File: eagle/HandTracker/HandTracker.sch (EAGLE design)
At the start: 29 parts, among them IC1 FT232RL, J1 ZX62-AB-5PA(31), U1 LSM9DS1TR, U2 MAX11629EEE+21-0055_E16+5_MXM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

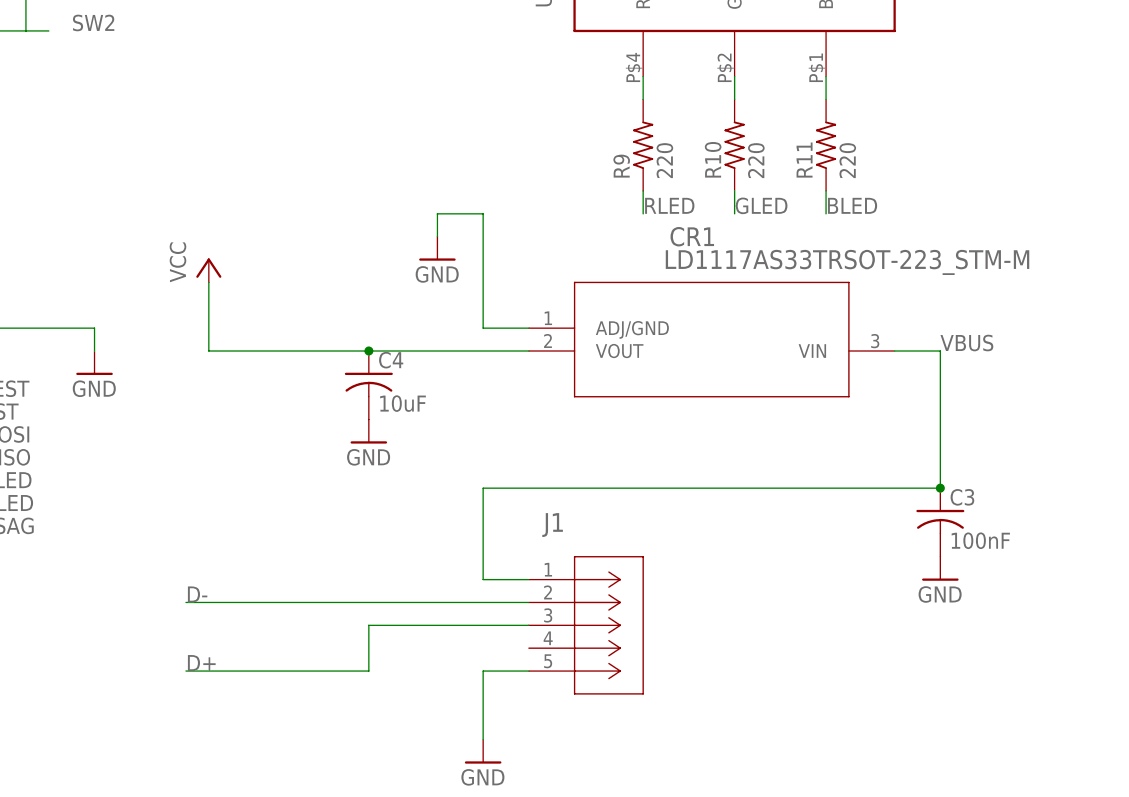
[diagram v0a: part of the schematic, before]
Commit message: Changed linear voltage regulator.
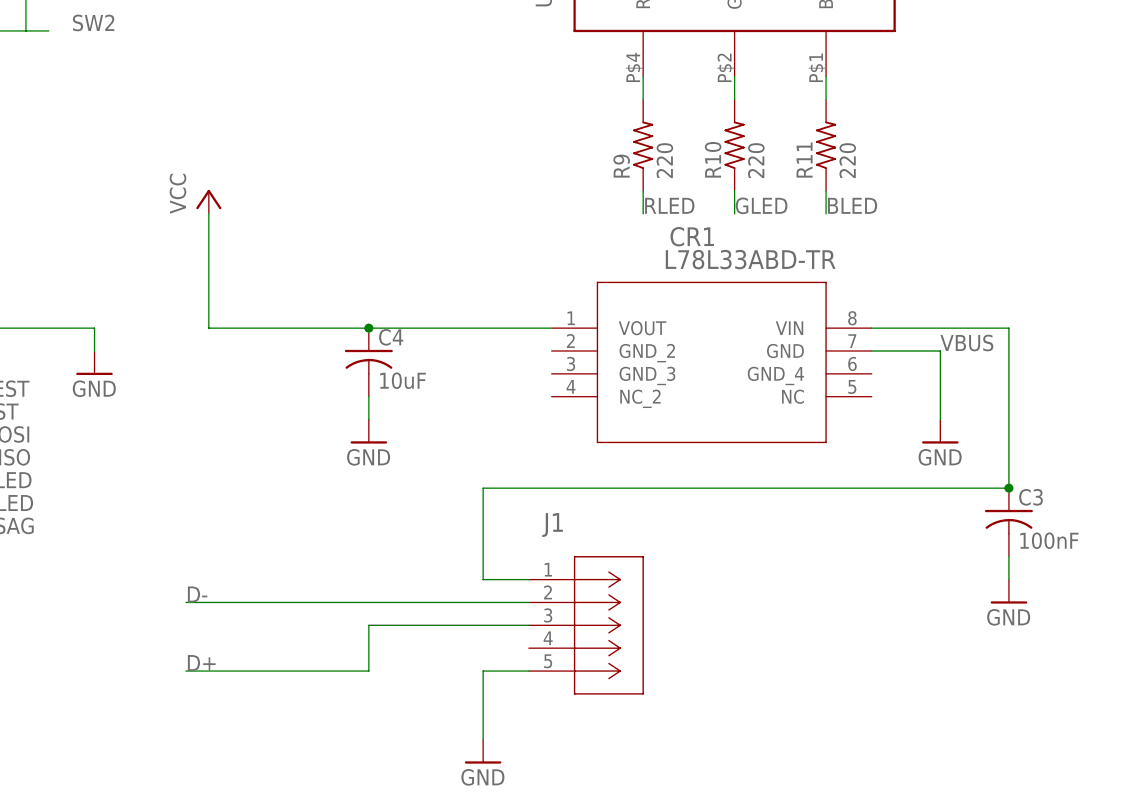
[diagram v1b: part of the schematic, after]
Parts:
- CR1: value LD1117AS33TRSOT-223_STM-M -> L78L33ABD-TR; device LD1117AS33TR:LD1117AS33TRSOT-223_STM-M -> Regulator:L78L33ABD-TR
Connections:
- net GND: now also CR1.GND; no longer CR1.ADJ/GND
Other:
- moved on the sheet: C3, C4
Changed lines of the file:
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@@
 <drawing>
 <settings>
-<setting alwaysvectorfont="no"/>
+<setting alwaysvectorfont="yes"/>
 <setting verticaltext="up"/>
 </settings>
@@
 <parts>
 <part name="U$1" library="ELEC327" deviceset="MSP430G2XX3" device="TSSOP"/>
-<part name="CR1" library="LD1117AS33TR" deviceset="LD1117AS33TR" device="SOT-223_STM-M"/>
 <part name="U1" library="LSM9DS1" deviceset="LSM9DS1TR" device=""/>
 <part name="U2" library="MAX11629EEE+" deviceset="MAX11629EEE+" device="21-0055_E16+5_MXM-M"/>
@@
 <part name="C9" library="rcl" library_urn="urn:adsk.eagle:library:334" deviceset="C-US" device="C1206" package3d_urn="urn:adsk.eagle:package:23618/2" value="10nF"/>
 <part name="GND15" library="supply1" library_urn="urn:adsk.eagle:library:371" deviceset="GND" device=""/>
+<part name="CR1" library="Regulator" deviceset="L78L33ABD-TR" device=""/>
 </parts>
 <sheets>
@@
 <attribute name="NAME" x="40.64" y="-33.02" size="1.778" layer="95"/>
 </instance>
-<instance part="CR1" gate="A" x="139.7" y="-10.16" smashed="yes">
-<attribute name="NAME" x="157.8356" y="-1.0414" size="2.0828" layer="95" ratio="6" rot="SR0"/>
-<attribute name="VALUE" x="157.2006" y="-3.5814" size="2.0828" layer="96" ratio="6" rot="SR0"/>
-</instance>
 <instance part="U1" gate="A" x="-66.04" y="-27.94" smashed="yes">
 <attribute name="NAME" x="-40.2844" y="-18.8214" size="2.0828" layer="95" ratio="6" rot="SR0"/>
@@
 <attribute name="VALUE" x="134.62" y="-60.96" size="1.778" layer="96"/>
 </instance>
-<instance part="GND2" gate="1" x="132.08" y="-2.54" smashed="yes">
-<attribute name="VALUE" x="129.54" y="-5.08" size="1.778" layer="96"/>
-</instance>
-<instance part="P+1" gate="VCC" x="106.68" y="-2.54" smashed="yes">
-<attribute name="VALUE" x="104.14" y="-5.08" size="1.778" layer="96" rot="R90"/>
+<instance part="GND2" gate="1" x="187.96" y="-22.86" smashed="yes">
+<attribute name="VALUE" x="185.42" y="-25.4" size="1.778" layer="96"/>
+</instance>
+<instance part="P+1" gate="VCC" x="106.68" y="5.08" smashed="yes">
+<attribute name="VALUE" x="104.14" y="2.54" size="1.778" layer="96" rot="R90"/>
 </instance>
 <instance part="P+2" gate="VCC" x="25.4" y="-5.08" smashed="yes">
@@
 <attribute name="VALUE" x="-5.08" y="17.78" size="1.778" layer="96"/>
 </instance>
-<instance part="C3" gate="G$1" x="187.96" y="-30.48" smashed="yes">
-<attribute name="NAME" x="188.976" y="-29.845" size="1.778" layer="95"/>
-<attribute name="VALUE" x="188.976" y="-34.671" size="1.778" layer="96"/>
-</instance>
-<instance part="GND9" gate="1" x="187.96" y="-38.1" smashed="yes">
-<attribute name="VALUE" x="185.42" y="-40.64" size="1.778" layer="96"/>
-</instance>
-<instance part="C4" gate="G$1" x="124.46" y="-15.24" smashed="yes">
-<attribute name="NAME" x="125.476" y="-14.605" size="1.778" layer="95"/>
-<attribute name="VALUE" x="125.476" y="-19.431" size="1.778" layer="96"/>
+<instance part="C3" gate="G$1" x="195.58" y="-30.48" smashed="yes">
+<attribute name="NAME" x="196.596" y="-29.845" size="1.778" layer="95"/>
+<attribute name="VALUE" x="196.596" y="-34.671" size="1.778" layer="96"/>
+</instance>
+<instance part="GND9" gate="1" x="195.58" y="-40.64" smashed="yes">
+<attribute name="VALUE" x="193.04" y="-43.18" size="1.778" layer="96"/>
+</instance>
+<instance part="C4" gate="G$1" x="124.46" y="-12.7" smashed="yes">
+<attribute name="NAME" x="125.476" y="-12.065" size="1.778" layer="95"/>
+<attribute name="VALUE" x="125.476" y="-16.891" size="1.778" layer="96"/>
 </instance>
 <instance part="GND10" gate="1" x="124.46" y="-22.86" smashed="yes">
@@
 <instance part="GND15" gate="1" x="10.16" y="-48.26" smashed="yes">
 <attribute name="VALUE" x="7.62" y="-50.8" size="1.778" layer="96"/>
+</instance>
+<instance part="CR1" gate="A" x="142.24" y="-10.16" smashed="yes">
+<attribute name="NAME" x="157.8356" y="-1.0414" size="2.0828" layer="95" ratio="6" rot="SR0"/>
+<attribute name="VALUE" x="157.2006" y="-3.5814" size="2.0828" layer="96" ratio="6" rot="SR0"/>
 </instance>
 </instances>
@@
 <nets>
 <net name="GND" class="0">
-<segment>
-<pinref part="CR1" gate="A" pin="ADJ/GND"/>
-<wire x1="142.24" y1="-10.16" x2="137.16" y2="-10.16" width="0.1524" layer="91"/>
-<wire x1="137.16" y1="-10.16" x2="137.16" y2="2.54" width="0.1524" layer="91"/>
-<wire x1="137.16" y1="2.54" x2="132.08" y2="2.54" width="0.1524" layer="91"/>
-<pinref part="GND2" gate="1" pin="GND"/>
-<wire x1="132.08" y1="2.54" x2="132.08" y2="0" width="0.1524" layer="91"/>
-</segment>
 <segment>
 <pinref part="J1" gate="A" pin="GND"/>
@@
 <pinref part="C3" gate="G$1" pin="2"/>
 <pinref part="GND9" gate="1" pin="GND"/>
+<wire x1="195.58" y1="-35.56" x2="195.58" y2="-38.1" width="0.1524" layer="91"/>
 </segment>
 <segment>
 <pinref part="C4" gate="G$1" pin="2"/>
 <pinref part="GND10" gate="1" pin="GND"/>
+<wire x1="124.46" y1="-17.78" x2="124.46" y2="-20.32" width="0.1524" layer="91"/>
 </segment>
 <segment>
@@
 <pinref part="GND15" gate="1" pin="GND"/>
 </segment>
+<segment>
+<pinref part="GND2" gate="1" pin="GND"/>
+<wire x1="187.96" y1="-20.32" x2="187.96" y2="-12.7" width="0.1524" layer="91"/>
+<pinref part="CR1" gate="A" pin="GND"/>
+<wire x1="187.96" y1="-12.7" x2="180.34" y2="-12.7" width="0.1524" layer="91"/>
+</segment>
 </net>
 <net name="VBUS" class="0">
@@
 <wire x1="142.24" y1="-38.1" x2="137.16" y2="-38.1" width="0.1524" layer="91"/>
 <wire x1="137.16" y1="-38.1" x2="137.16" y2="-27.94" width="0.1524" layer="91"/>
-<wire x1="137.16" y1="-27.94" x2="187.96" y2="-27.94" width="0.1524" layer="91"/>
+<wire x1="137.16" y1="-27.94" x2="195.58" y2="-27.94" width="0.1524" layer="91"/>
+<wire x1="195.58" y1="-27.94" x2="195.58" y2="-10.16" width="0.1524" layer="91"/>
+<wire x1="195.58" y1="-10.16" x2="180.34" y2="-10.16" width="0.1524" layer="91"/>
+<pinref part="C3" gate="G$1" pin="1"/>
+<junction x="195.58" y="-27.94"/>
+<label x="187.96" y="-12.7" size="1.778" layer="95"/>
 <pinref part="CR1" gate="A" pin="VIN"/>
-<wire x1="187.96" y1="-27.94" x2="187.96" y2="-12.7" width="0.1524" layer="91"/>
-<wire x1="187.96" y1="-12.7" x2="182.88" y2="-12.7" width="0.1524" layer="91"/>
-<pinref part="C3" gate="G$1" pin="1"/>
-<junction x="187.96" y="-27.94"/>
-<label x="187.96" y="-12.7" size="1.778" layer="95"/>
 </segment>
 <segment>
@@
 <segment>
 <pinref part="P+1" gate="VCC" pin="VCC"/>
-<wire x1="106.68" y1="-5.08" x2="106.68" y2="-12.7" width="0.1524" layer="91"/>
+<wire x1="106.68" y1="2.54" x2="106.68" y2="-10.16" width="0.1524" layer="91"/>
+<wire x1="106.68" y1="-10.16" x2="124.46" y2="-10.16" width="0.1524" layer="91"/>
+<pinref part="C4" gate="G$1" pin="1"/>
+<wire x1="124.46" y1="-10.16" x2="144.78" y2="-10.16" width="0.1524" layer="91"/>
+<junction x="124.46" y="-10.16"/>
 <pinref part="CR1" gate="A" pin="VOUT"/>
-<wire x1="106.68" y1="-12.7" x2="124.46" y2="-12.7" width="0.1524" layer="91"/>
-<pinref part="C4" gate="G$1" pin="1"/>
-<wire x1="124.46" y1="-12.7" x2="142.24" y2="-12.7" width="0.1524" layer="91"/>
-<junction x="124.46" y="-12.7"/>
-</segment>
-<segment>
+</segment>
+<segment>

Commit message: Fix LED and route planes.
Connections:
- new net BLED_RES: R11.2, U$2.BLUE
- new net GLED_RES: R10.2, U$2.GREEN
- new net RLED_RES: R9.2, U$2.RED
- net BLED: no longer R11.2, U$2.BLUE
- net DEN_AG: now also U$1.2
- net GLED: no longer R10.2, U$2.GREEN
- net RLED: no longer R9.2, U$2.RED
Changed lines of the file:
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@@
 <label x="-10.16" y="-58.42" size="1.778" layer="95"/>
+</segment>
+<segment>
+<pinref part="U$1" gate="G$1" pin="2"/>
+<wire x1="30.48" y1="-12.7" x2="27.94" y2="-12.7" width="0.1524" layer="91"/>
+<label x="22.86" y="-12.7" size="1.778" layer="95"/>
 </segment>
 </net>
@@
 </segment>
 <segment>
-<pinref part="U$2" gate="G$1" pin="RED"/>
-<wire x1="154.94" y1="17.78" x2="154.94" y2="15.24" width="0.1524" layer="91"/>
-<pinref part="R9" gate="G$1" pin="2"/>
-</segment>
-<segment>
 <pinref part="R9" gate="G$1" pin="1"/>
 <wire x1="154.94" y1="5.08" x2="154.94" y2="2.54" width="0.1524" layer="91"/>
@@
 </segment>
 <segment>
-<pinref part="U$2" gate="G$1" pin="GREEN"/>
-<wire x1="165.1" y1="17.78" x2="165.1" y2="15.24" width="0.1524" layer="91"/>
-<pinref part="R10" gate="G$1" pin="2"/>
-</segment>
-<segment>
 <pinref part="R10" gate="G$1" pin="1"/>
 <wire x1="165.1" y1="5.08" x2="165.1" y2="2.54" width="0.1524" layer="91"/>
@@
 <wire x1="30.48" y1="-33.02" x2="27.94" y2="-33.02" width="0.1524" layer="91"/>
 <label x="25.4" y="-33.02" size="1.778" layer="95"/>
-</segment>
-<segment>
-<pinref part="U$2" gate="G$1" pin="BLUE"/>
-<wire x1="175.26" y1="17.78" x2="175.26" y2="15.24" width="0.1524" layer="91"/>
-<pinref part="R11" gate="G$1" pin="2"/>
 </segment>
 <segment>
@@
 </segment>
 </net>
+<net name="RLED_RES" class="0">
+<segment>
+<pinref part="U$2" gate="G$1" pin="RED"/>
+<wire x1="154.94" y1="17.78" x2="154.94" y2="15.24" width="0.1524" layer="91"/>
+<pinref part="R9" gate="G$1" pin="2"/>
+<label x="149.86" y="10.16" size="1.778" layer="95" rot="R90"/>
+</segment>
+</net>
+<net name="GLED_RES" class="0">
+<segment>
+<pinref part="U$2" gate="G$1" pin="GREEN"/>
+<wire x1="165.1" y1="17.78" x2="165.1" y2="15.24" width="0.1524" layer="91"/>
+<pinref part="R10" gate="G$1" pin="2"/>
+<label x="162.56" y="10.16" size="1.778" layer="95" rot="R90"/>
+</segment>
+</net>
+<net name="BLED_RES" class="0">
+<segment>
+<pinref part="U$2" gate="G$1" pin="BLUE"/>
+<wire x1="175.26" y1="17.78" x2="175.26" y2="15.24" width="0.1524" layer="91"/>
+<pinref part="R11" gate="G$1" pin="2"/>
+<label x="172.72" y="10.16" size="1.778" layer="95" rot="R90"/>
+</segment>
+</net>

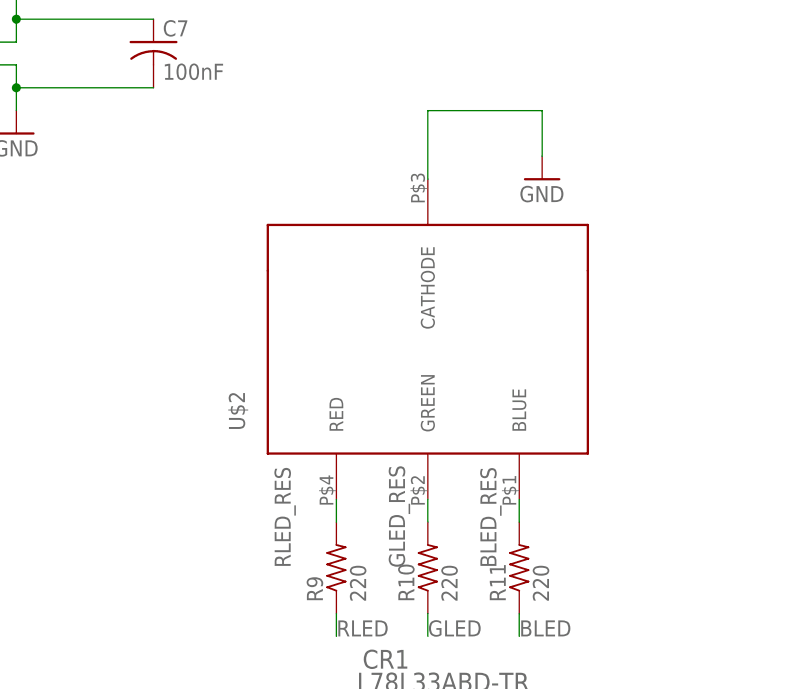
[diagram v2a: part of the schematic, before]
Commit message: replaced rgb led with three LEDs
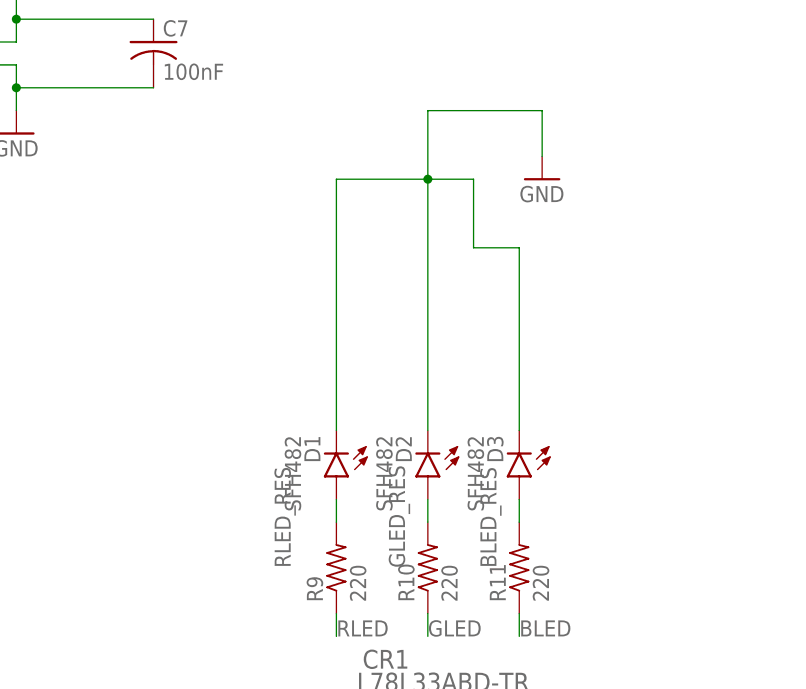
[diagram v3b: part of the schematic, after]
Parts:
- removed U$2: NTE30158, RGB LED:NTE30158
- added D1, D2, D3: SFH482, led:SFH482
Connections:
- net BLED_RES: now also D3.A; no longer U$2.BLUE
- net GLED_RES: now also D2.A; no longer U$2.GREEN
- net GND: now also D1.C, D2.C, D3.C; no longer U$2.CATHODE
- net RLED_RES: now also D1.A; no longer U$2.RED
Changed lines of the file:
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@@
 <drawing>
 <settings>
-<setting alwaysvectorfont="yes"/>
+<setting alwaysvectorfont="no"/>
 <setting verticaltext="up"/>
 </settings>
@@
 <part name="R3" library="rcl" library_urn="urn:adsk.eagle:library:334" deviceset="R-US_" device="R1206" package3d_urn="urn:adsk.eagle:package:23540/2" value="10k"/>
 <part name="P+13" library="supply1" library_urn="urn:adsk.eagle:library:371" deviceset="VCC" device=""/>
-<part name="U$2" library="RGB LED" deviceset="NTE30158" device=""/>
 <part name="GND14" library="supply1" library_urn="urn:adsk.eagle:library:371" deviceset="GND" device=""/>
 <part name="R9" library="rcl" library_urn="urn:adsk.eagle:library:334" deviceset="R-US_" device="R1206" package3d_urn="urn:adsk.eagle:package:23540/2" value="220"/>
@@
 <part name="GND15" library="supply1" library_urn="urn:adsk.eagle:library:371" deviceset="GND" device=""/>
 <part name="CR1" library="Regulator" deviceset="L78L33ABD-TR" device=""/>
+<part name="D1" library="led" library_urn="urn:adsk.eagle:library:259" deviceset="SFH482" device="" package3d_urn="urn:adsk.eagle:package:15795/1"/>
+<part name="D2" library="led" library_urn="urn:adsk.eagle:library:259" deviceset="SFH482" device="" package3d_urn="urn:adsk.eagle:package:15795/1"/>
+<part name="D3" library="led" library_urn="urn:adsk.eagle:library:259" deviceset="SFH482" device="" package3d_urn="urn:adsk.eagle:package:15795/1"/>
 </parts>
 <sheets>
@@
 <attribute name="VALUE" x="-33.02" y="60.96" size="1.778" layer="96" rot="R90"/>
 </instance>
-<instance part="U$2" gate="G$1" x="147.32" y="22.86" smashed="yes">
-<attribute name="NAME" x="144.78" y="25.4" size="1.778" layer="95" rot="R90"/>
-</instance>
 <instance part="GND14" gate="1" x="177.8" y="53.34" smashed="yes">
 <attribute name="VALUE" x="175.26" y="50.8" size="1.778" layer="96"/>
@@
 <attribute name="NAME" x="157.8356" y="-1.0414" size="2.0828" layer="95" ratio="6" rot="SR0"/>
 <attribute name="VALUE" x="157.2006" y="-3.5814" size="2.0828" layer="96" ratio="6" rot="SR0"/>
+</instance>
+<instance part="D1" gate="1" x="154.94" y="20.32" smashed="yes" rot="R180">
+<attribute name="NAME" x="151.384" y="24.892" size="1.778" layer="95" rot="R270"/>
+<attribute name="VALUE" x="149.225" y="24.892" size="1.778" layer="96" rot="R270"/>
+</instance>
+<instance part="D2" gate="1" x="165.1" y="20.32" smashed="yes" rot="R180">
+<attribute name="NAME" x="161.544" y="24.892" size="1.778" layer="95" rot="R270"/>
+<attribute name="VALUE" x="159.385" y="24.892" size="1.778" layer="96" rot="R270"/>
+</instance>
+<instance part="D3" gate="1" x="175.26" y="20.32" smashed="yes" rot="R180">
+<attribute name="NAME" x="171.704" y="24.892" size="1.778" layer="95" rot="R270"/>
+<attribute name="VALUE" x="169.545" y="24.892" size="1.778" layer="96" rot="R270"/>
 </instance>
 </instances>
@@
 <wire x1="177.8" y1="55.88" x2="177.8" y2="60.96" width="0.1524" layer="91"/>
 <wire x1="177.8" y1="60.96" x2="165.1" y2="60.96" width="0.1524" layer="91"/>
-<pinref part="U$2" gate="G$1" pin="CATHODE"/>
 <wire x1="165.1" y1="60.96" x2="165.1" y2="53.34" width="0.1524" layer="91"/>
+<pinref part="D1" gate="1" pin="C"/>
+<wire x1="154.94" y1="25.4" x2="154.94" y2="53.34" width="0.1524" layer="91"/>
+<wire x1="154.94" y1="53.34" x2="165.1" y2="53.34" width="0.1524" layer="91"/>
+<pinref part="D2" gate="1" pin="C"/>
+<wire x1="165.1" y1="25.4" x2="165.1" y2="53.34" width="0.1524" layer="91"/>
+<junction x="165.1" y="53.34"/>
+<pinref part="D3" gate="1" pin="C"/>
+<wire x1="175.26" y1="25.4" x2="175.26" y2="45.72" width="0.1524" layer="91"/>
+<wire x1="175.26" y1="45.72" x2="170.18" y2="45.72" width="0.1524" layer="91"/>
+<wire x1="170.18" y1="45.72" x2="170.18" y2="53.34" width="0.1524" layer="91"/>
+<wire x1="170.18" y1="53.34" x2="165.1" y2="53.34" width="0.1524" layer="91"/>
 </segment>
 <segment>
@@
 <net name="RLED_RES" class="0">
 <segment>
-<pinref part="U$2" gate="G$1" pin="RED"/>
-<wire x1="154.94" y1="17.78" x2="154.94" y2="15.24" width="0.1524" layer="91"/>
 <pinref part="R9" gate="G$1" pin="2"/>
 <label x="149.86" y="10.16" size="1.778" layer="95" rot="R90"/>
+<pinref part="D1" gate="1" pin="A"/>
+<wire x1="154.94" y1="17.78" x2="154.94" y2="15.24" width="0.1524" layer="91"/>
 </segment>
 </net>
 <net name="GLED_RES" class="0">
 <segment>
-<pinref part="U$2" gate="G$1" pin="GREEN"/>
 <wire x1="165.1" y1="17.78" x2="165.1" y2="15.24" width="0.1524" layer="91"/>
 <pinref part="R10" gate="G$1" pin="2"/>
 <label x="162.56" y="10.16" size="1.778" layer="95" rot="R90"/>
+<pinref part="D2" gate="1" pin="A"/>
 </segment>
 </net>
 <net name="BLED_RES" class="0">
 <segment>
-<pinref part="U$2" gate="G$1" pin="BLUE"/>
 <wire x1="175.26" y1="17.78" x2="175.26" y2="15.24" width="0.1524" layer="91"/>
 <pinref part="R11" gate="G$1" pin="2"/>
 <label x="172.72" y="10.16" size="1.778" layer="95" rot="R90"/>
-</segment>
-</net>
+<pinref part="D3" gate="1" pin="A"/>
+</segment>
+</net>
